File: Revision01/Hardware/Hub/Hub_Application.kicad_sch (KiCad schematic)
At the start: 81 parts, among them J10 IDC 6Pin Male Header, J11 IDC 6Pin Male Header, J12 IDC 6Pin Male Header, J13 IDC 6Pin Male Header, J14 IDC 6Pin Male Header, J15 IDC 6Pin Female Socket, J16 IDC 6Pin Male Header, J17 IDC 6Pin Female Socket, J18 IDC 6Pin Female Socket, J19 SMA-J-P-H-ST-EM1, J6 IDC 6Pin Male Header, J7 IDC 6Pin Male Header, J8 IDC 6Pin Male Header, J9 IDC 6Pin Male Header, Q1 PMOS, Q2 NMOS, Q3 PMOS, U3 MPU-6500, U4 Adafruit 3070

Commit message: . Merged Amplifier & Hub libraries into "Lib" . Added Amplifier 6 pin IDC footprint . Finalized Amplifier layout & silkscreen
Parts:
- J10, J11, J12, J13, J14, J16, J6, J7, J8, J9: footprint Hub:AdamTech_BHR-06-VUA -> Lib:AdamTech_BHR-06-VUA; symbol Hub:IDC_6Pin_Male_Header -> Lib:IDC_6Pin_Male_Header
- J15, J17, J18: symbol Hub:IDC_6Pin_Female_Socket -> Lib:IDC_6Pin_Female_Socket
- J19: symbol Hub:ANT_SMA_Edge -> Lib:ANT_SMA_Edge
- R10: symbol Hub:StrainGaugeFullBridge -> Lib:StrainGaugeFullBridge
- U3: footprint Hub:MPU-6500_QFN40P300X300X95-25N -> Lib:MPU-6500_QFN40P300X300X95-25N; symbol Hub:MPU-6500 -> Lib:MPU-6500
- U4: footprint Hub:Adafruit3070 -> Lib:Adafruit3070; symbol Hub:Adafruit3070 -> Lib:Adafruit3070
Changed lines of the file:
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@@
 	)
 	(symbol
-		(lib_id "Hub:IDC_6Pin_Male_Header")
+		(lib_id "Lib:IDC_6Pin_Male_Header")
 		(at 163.83 199.39 0)
 		(unit 1)
@@
 			)
 		)
-		(property "Footprint" "Hub:AdamTech_BHR-06-VUA"
+		(property "Footprint" "Lib:AdamTech_BHR-06-VUA"
 			(at 163.83 199.39 0)
 			(effects
@@
 	)
 	(symbol
-		(lib_id "Hub:IDC_6Pin_Male_Header")
+		(lib_id "Lib:IDC_6Pin_Male_Header")
 		(at 148.59 118.11 0)
 		(unit 1)
@@
 			)
 		)
-		(property "Footprint" "Hub:AdamTech_BHR-06-VUA"
+		(property "Footprint" "Lib:AdamTech_BHR-06-VUA"
 			(at 148.59 118.11 0)
 			(effects
@@
 	)
 	(symbol
-		(lib_id "Hub:IDC_6Pin_Male_Header")
+		(lib_id "Lib:IDC_6Pin_Male_Header")
 		(at 148.59 80.01 0)
 		(unit 1)
@@
 			)
 		)
-		(property "Footprint" "Hub:AdamTech_BHR-06-VUA"
+		(property "Footprint" "Lib:AdamTech_BHR-06-VUA"
 			(at 148.59 80.01 0)
 			(effects
@@
 	)
 	(symbol
-		(lib_id "Hub:IDC_6Pin_Male_Header")
+		(lib_id "Lib:IDC_6Pin_Male_Header")
 		(at 148.59 105.41 0)
 		(unit 1)
@@
 			)
 		)
-		(property "Footprint" "Hub:AdamTech_BHR-06-VUA"
+		(property "Footprint" "Lib:AdamTech_BHR-06-VUA"
 			(at 148.59 105.41 0)
 			(effects
@@
 	)
 	(symbol
-		(lib_id "Hub:ANT_SMA_Edge")
+		(lib_id "Lib:ANT_SMA_Edge")
 		(at 349.25 203.2 0)
 		(unit 1)
@@
 	)
 	(symbol
-		(lib_id "Hub:Adafruit3070")
+		(lib_id "Lib:Adafruit3070")
 		(at 285.75 179.07 0)
 		(unit 1)
@@
 			)
 		)
-		(property "Footprint" "Hub:Adafruit3070"
+		(property "Footprint" "Lib:Adafruit3070"
 			(at 285.75 179.07 0)
 			(effects
@@
 	)
 	(symbol
-		(lib_id "Hub:IDC_6Pin_Male_Header")
+		(lib_id "Lib:IDC_6Pin_Male_Header")
 		(at 148.59 168.91 0)
 		(unit 1)
@@
 			)
 		)
-		(property "Footprint" "Hub:AdamTech_BHR-06-VUA"
+		(property "Footprint" "Lib:AdamTech_BHR-06-VUA"
 			(at 148.59 168.91 0)
 			(effects
@@
 	)
 	(symbol
-		(lib_id "Hub:StrainGaugeFullBridge")
+		(lib_id "Lib:StrainGaugeFullBridge")
 		(at 146.05 57.15 0)
 		(unit 1)
@@
 	)
 	(symbol
-		(lib_id "Hub:IDC_6Pin_Male_Header")
+		(lib_id "Lib:IDC_6Pin_Male_Header")
 		(at 199.39 199.39 0)
 		(unit 1)
@@
 			)
 		)
-		(property "Footprint" "Hub:AdamTech_BHR-06-VUA"
+		(property "Footprint" "Lib:AdamTech_BHR-06-VUA"
 			(at 199.39 199.39 0)
 			(effects
@@
 	)
 	(symbol
-		(lib_id "Hub:IDC_6Pin_Female_Socket")
+		(lib_id "Lib:IDC_6Pin_Female_Socket")
 		(at 181.61 199.39 0)
 		(mirror y)
@@
 	)
 	(symbol
-		(lib_id "Hub:IDC_6Pin_Male_Header")
+		(lib_id "Lib:IDC_6Pin_Male_Header")
 		(at 148.59 143.51 0)
 		(unit 1)
@@
 			)
 		)
-		(property "Footprint" "Hub:AdamTech_BHR-06-VUA"
+		(property "Footprint" "Lib:AdamTech_BHR-06-VUA"
 			(at 148.59 143.51 0)
 			(effects
@@
 	)
 	(symbol
-		(lib_id "Hub:MPU-6500")
+		(lib_id "Lib:MPU-6500")
 		(at 321.31 110.49 0)
 		(unit 1)
@@
 			)
 		)
-		(property "Footprint" "Hub:MPU-6500_QFN40P300X300X95-25N"
+		(property "Footprint" "Lib:MPU-6500_QFN40P300X300X95-25N"
 			(at 321.31 93.98 0)
 			(effects
@@
 	)
 	(symbol
-		(lib_id "Hub:IDC_6Pin_Female_Socket")
+		(lib_id "Lib:IDC_6Pin_Female_Socket")
 		(at 218.44 199.39 0)
 		(mirror y)
@@
 	)
 	(symbol
-		(lib_id "Hub:IDC_6Pin_Male_Header")
+		(lib_id "Lib:IDC_6Pin_Male_Header")
 		(at 148.59 92.71 0)
 		(unit 1)
@@
 			)
 		)
-		(property "Footprint" "Hub:AdamTech_BHR-06-VUA"
+		(property "Footprint" "Lib:AdamTech_BHR-06-VUA"
 			(at 148.59 92.71 0)
 			(effects
@@
 	)
 	(symbol
-		(lib_id "Hub:IDC_6Pin_Male_Header")
+		(lib_id "Lib:IDC_6Pin_Male_Header")
 		(at 148.59 156.21 0)
 		(unit 1)
@@
 			)
 		)
-		(property "Footprint" "Hub:AdamTech_BHR-06-VUA"
+		(property "Footprint" "Lib:AdamTech_BHR-06-VUA"
 			(at 148.59 156.21 0)
 			(effects
@@
 	)
 	(symbol
-		(lib_id "Hub:IDC_6Pin_Female_Socket")
+		(lib_id "Lib:IDC_6Pin_Female_Socket")
 		(at 231.14 199.39 0)
 		(unit 1)
@@
 	)
 	(symbol
-		(lib_id "Hub:IDC_6Pin_Male_Header")
+		(lib_id "Lib:IDC_6Pin_Male_Header")
 		(at 148.59 130.81 0)
 		(unit 1)
@@
 			)
 		)
-		(property "Footprint" "Hub:AdamTech_BHR-06-VUA"
+		(property "Footprint" "Lib:AdamTech_BHR-06-VUA"
 			(at 148.59 130.81 0)
 			(effects

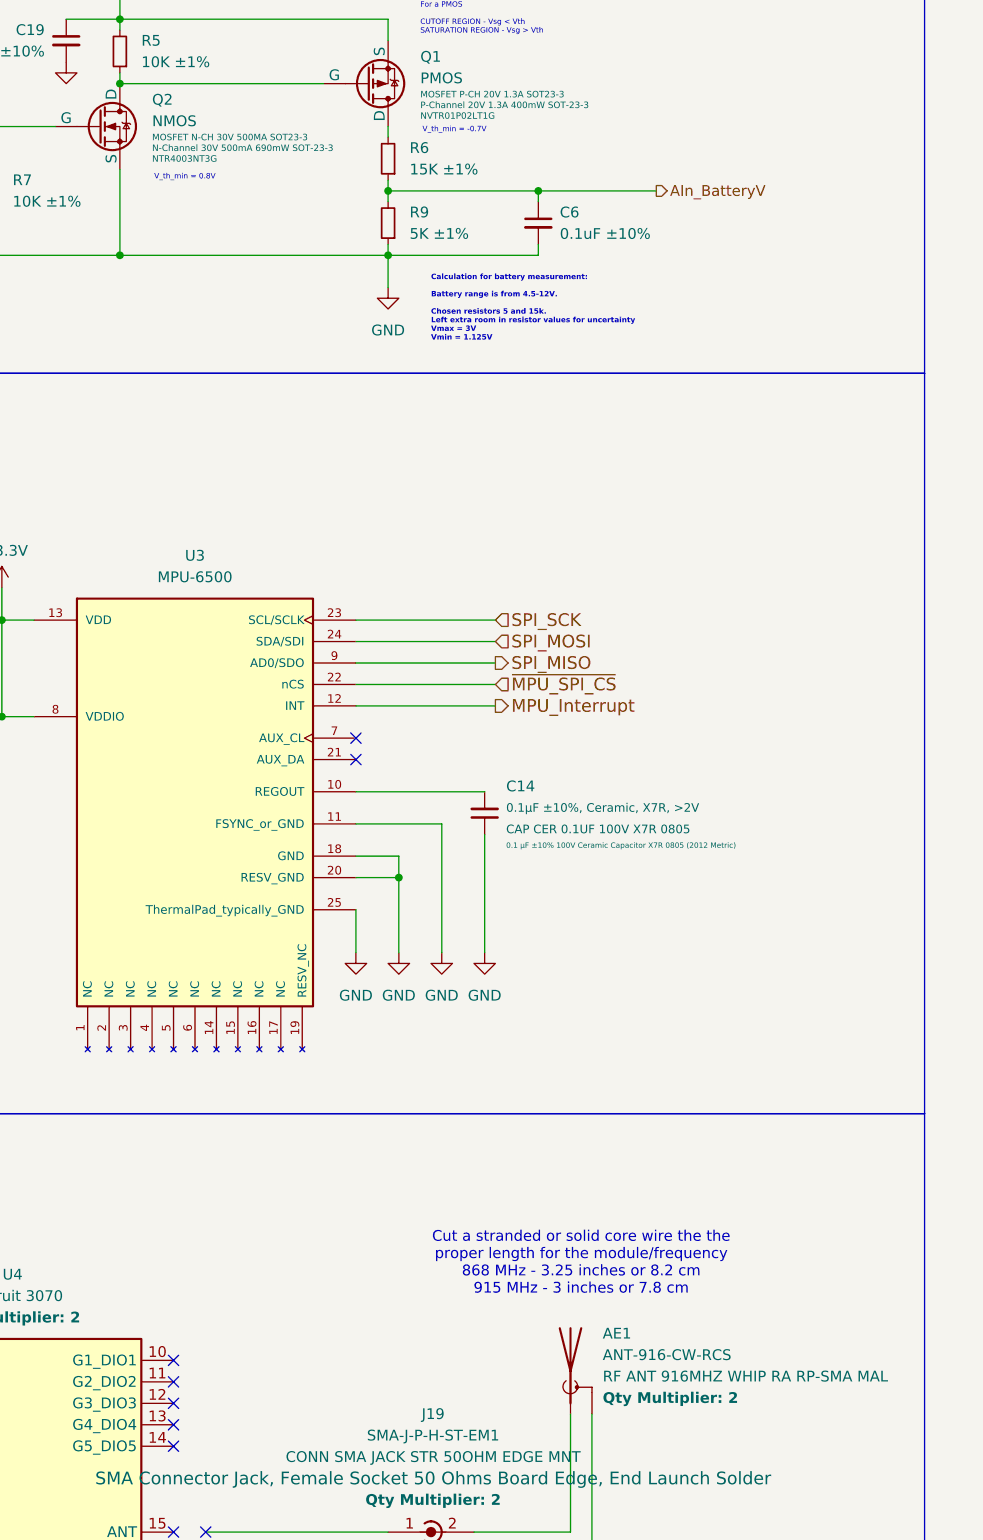
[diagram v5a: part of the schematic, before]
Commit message: . Fixed major BOM bug in Antenna, ordering correct Male Outer, Male Inner Part . Added Mouser column in Hub.
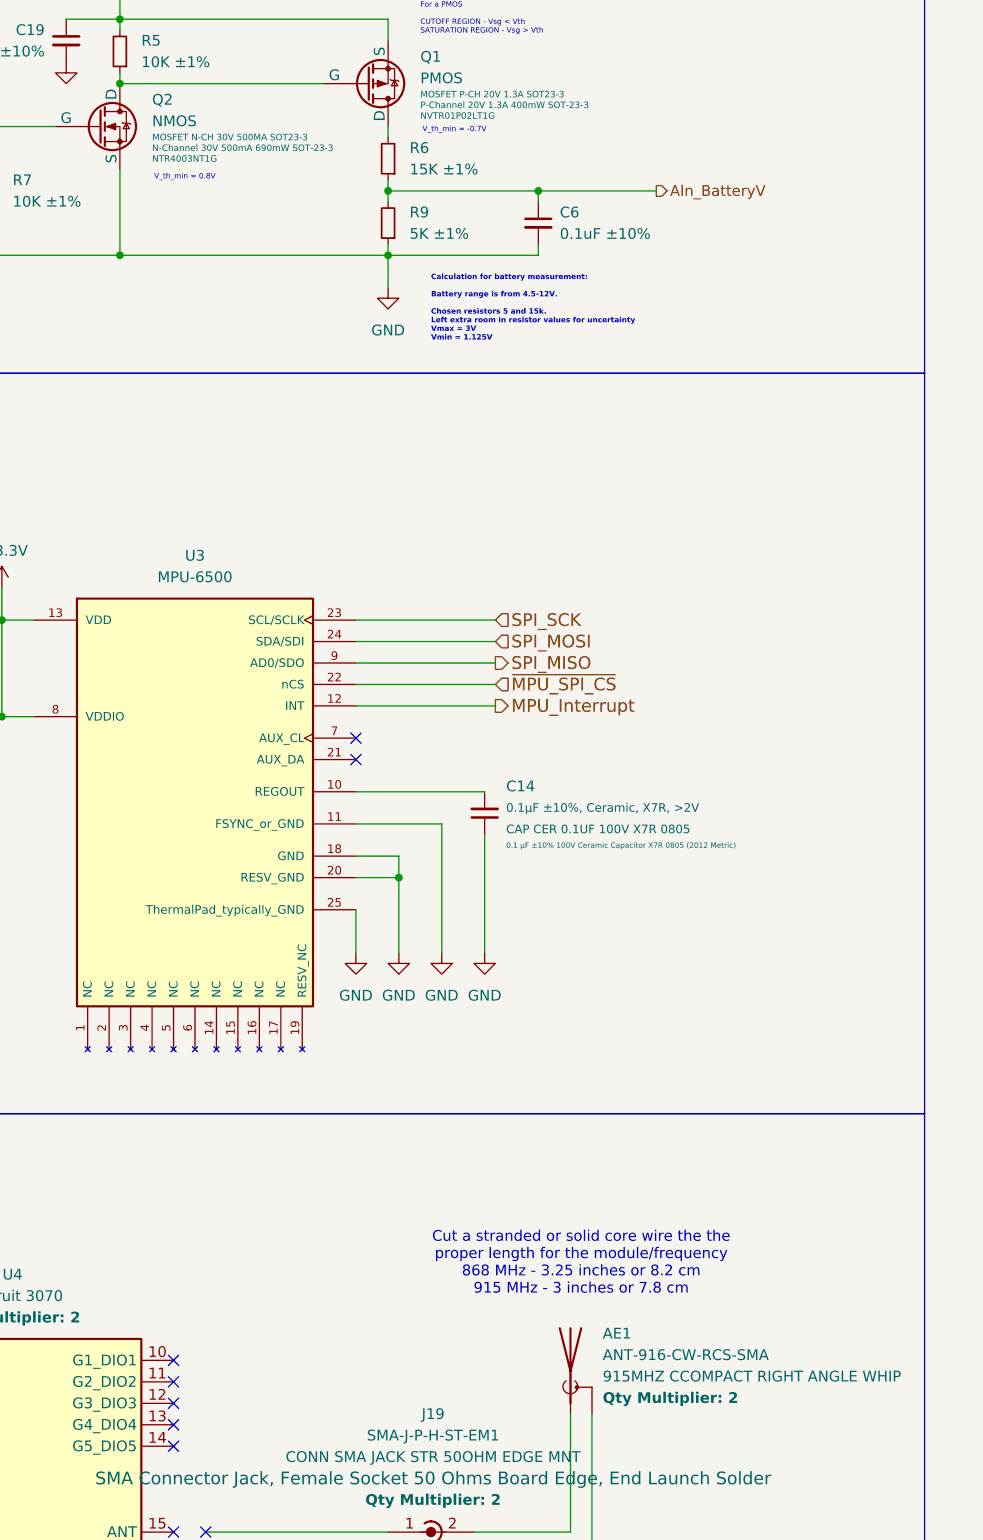
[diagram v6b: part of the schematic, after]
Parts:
- AE1: value ANT-916-CW-RCS -> ANT-916-CW-RCS-SMA; Detailed Description RF ANTENNA ISM, LoRa, Sensor Networks, SigFox Whip, Right A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 -> RF ANTENNA ISM, LoRaWAN, LPWA Whip, Right Angle SMA Male Co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; DigiKey Link https://www.digikey.ca/en/products/detail/te-connectivity-linx/ANT-916-CW-RCS/340139 -> https://www.digikey.ca/en/products/detail/te-connectivity-linx/ANT-916-CW-RCS-SMA/16630288?s=N4IgTCBcDaIIIDkAqBaAnARgGwoMIHUUAlXAZRVIFk4QBdAXyA; DigiKey Part Number ANT-916-CW-RCS-ND -> 343-ANT-916-CW-RCS-SMA-ND; Manufacturer Part Number ANT-916-CW-RCS -> ANT-916-CW-RCS-SMA; Mouser Link (none) -> https://www.mouser.ca/ProductDetail/TE-Connectivity-Linx-Te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; Mouser Part Number (none) -> 712-ANT-916-CWRCSSMA
- C1, C19: Mouser Link (none) -> https://www.mouser.ca/ProductDetail/Samsung-Electro-Mechani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; Mouser Part Number (none) -> 187-CL31A226KAHNNNE
- C10, C14, C6, C7: Mouser Link (none) -> https://www.mouser.ca/ProductDetail/Samsung-Electro-Mechani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; Mouser Part Number (none) -> 187-CL21B104KCFNNNE
- C12: Mouser Link (none) -> https://www.mouser.ca/ProductDetail/Samsung-Electro-Mechani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; Mouser Part Number (none) -> 187-CL10B103KB8WPND
- D1, D10, D11, D12, D13, D14, D15, D16, D2, D3, D4, D5, D6, D7, D8, D9: Mouser Link (none) -> https://www.mouser.ca/ProductDetail/Diodes-Incorporated/DDZ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; Mouser Part Number (none) -> 621-DDZ9684-7
- F2, F3, F4, F5, F6, F7, F8, F9: Mouser Link (none) -> https://www.mouser.ca/ProductDetail/KYOCERA-AVX/F0603G0R02F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; Mouser Part Number (none) -> 581-F0603G0R02FNTR
- J10, J11, J12, J13, J14, J16, J6, J7, J8, J9: Mouser Link (none) -> https://www.mouser.ca/ProductDetail/Adam-Tech/BHR-06-VUA?qs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; Mouser Part Number (none) -> 737-BHR-06-VUA
- J15, J17, J18: Mouser Link (none) -> https://www.mouser.ca/ProductDetail/Adam-Tech/FCS-06-SG?qs=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; Mouser Part Number (none) -> 737-FCS-06-SG
- J19: Mouser Link (none) -> https://www.mouser.ca/ProductDetail/Samtec/SMA-J-P-H-ST-EM1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; Mouser Part Number (none) -> SMA-J-P-H-ST-EM1
- Q1: Mouser Link (none) -> https://www.mouser.ca/ProductDetail/onsemi/NVTR01P02LT1G?qs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; Mouser Part Number (none) -> 863-NVTR01P02LT1G
- Q2: Manufacturer Part Number NTR4003NT3G -> NTR4003NT1G; Mouser Link (none) -> https://www.mouser.ca/ProductDetail/onsemi/NTR4003NT1G?qs=C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; Mouser Part Number (none) -> 863-NTR4003NT1G
- Q3: Mouser Link (none) -> https://www.mouser.ca/ProductDetail/Diodes-Incorporated/ZXM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; Mouser Part Number (none) -> 522-ZXMP10A13FTA
- R11, R13, R15, R17, R19, R2, R21, R23: Mouser Link (none) -> https://www.mouser.ca/ProductDetail/Vishay/CRCW0805100RFKEA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; Mouser Part Number (none) -> 71-CRCW0805-100-E3
- R12, R14, R16, R18, R20, R22, R24, R26: Mouser Link (none) -> https://www.mouser.ca/ProductDetail/Vishay/CRCW08051M00FKEA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; Mouser Part Number (none) -> 71-CRCW0805-1.0M-E3
- R5, R7, R8: Mouser Link (none) -> https://www.mouser.ca/ProductDetail/Vishay/CRCW080510K0FKEA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; Mouser Part Number (none) -> 71-CRCW0805-10K-E3
- R6: Mouser Link (none) -> https://www.mouser.ca/ProductDetail/Vishay/CRCW080515K0FKEA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; Mouser Part Number (none) -> 71-CRCW0805-15K-E3
- R9: Mouser Link (none) -> https://www.mouser.ca/ProductDetail/Vishay/CRCW08055K00FKTA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; Mouser Part Number (none) -> 71-CRCW0805-5K
- U3: Mouser Link (none) -> https://www.mouser.ca/ProductDetail/TDK-InvenSense/MPU-6500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; Mouser Part Number (none) -> 410-MPU-6500
- U4: Mouser Link (none) -> https://www.mouser.ca/ProductDetail/Adafruit/3070?qs=AGnqjq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; Mouser Part Number (none) -> 485-3070

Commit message: . Exported BOM (.csv), gerbers & dill files, 3D Model (.step) file to Product/2025-08-16 for both Amplifier & Hub boards.
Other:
- company: BCIT BAJA -> BCIT Racing
- title: Peripherals -> Hub
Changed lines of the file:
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@@
 	(paper "A3")
 	(title_block
-		(title "Peripherals")
-		(date "2025-03-08")
-		(rev "1")
-		(company "BCIT BAJA")
+		(title "Hub")
+		(date "2025-08-16")
+		(rev "01")
+		(company "BCIT Racing")
+		(comment 1 "Parry Zhuo & Daniel Mahmoud")
 	)
 	(rectangle

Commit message: . Made sure amplifier passive silk screen doesn't overlap pads . Added 6xAA battery holder to hub BOM . Exported gerbers, drl files .zip (PCBWay approved)
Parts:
- C1, C19: DigiKey Part Number 1276-3047-1-ND - Cut Tape (CT) -> 1276-3047-1-ND
- C10, C14: value 0.1µF ±10%, Ceramic, X7R, >2V -> 0.1uF ±10%, X7R; DigiKey Part Number 1276-6840-1-ND - Cut Tape (CT) -> 1276-6840-1-ND
- C11, C13, C15, C16, C17, C18, C8, C9: DigiKey Link (none) -> https://www.digikey.ca/en/products/detail/samsung-electro-m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; DigiKey Part Number (none) -> 1276-1185-2-ND
- C12: DigiKey Part Number 1276-CL10B103KB8WPNDCT-ND - Cut Tape (CT) -> 1276-CL10B103KB8WPNDCT-ND
- C6, C7: value 0.1uF ±10% -> 0.1uF ±10%, X7R; DigiKey Part Number 1276-6840-1-ND - Cut Tape (CT) -> 1276-6840-1-ND
- F2, F3, F4, F5, F6, F7, F8, F9: DigiKey Part Number 478-13097-1-ND - Cut Tape (CT) -> 478-13097-1-ND
- J19: value SMA-J-P-H-ST-EM1 -> CON-SMA-EDGE-S; Detailed Description SMA Connector Jack, Female Socket 50 Ohms Board Edge, End L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 -> SMA Connector Jack, Female Socket Board Edge, End Launch So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; DigiKey Link https://www.digikey.ca/en/products/detail/samtec-inc/SMA-J-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 -> https://www.digikey.ca/en/products/detail/rf-solutions/CON-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; DigiKey Part Number SAM8857-ND -> CON-SMA-EDGE-S-ND; Manufacturer Samtec Inc. -> RF Solutions; Manufacturer Part Number SMA-J-P-H-ST-EM1 -> CON-SMA-EDGE-S; Mouser Link https://www.mouser.ca/ProductDetail/Samtec/SMA-J-P-H-ST-EM1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 -> https://www.mouser.ca/ProductDetail/RF-Solutions/CON-SMA-ED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; Mouser Part Number SMA-J-P-H-ST-EM1 -> 223-CON-SMA-EDGE-S
- Q2: DigiKey Part Number NTR4003NT3GOSCT-ND - Cut Tape (CT) -> NTR4003NT3GOSCT-ND
- R10: DigiKey Link https://www.aliexpress.com/item/1005006546478858.html -> (none)
- R11, R13, R15, R17, R19, R2, R21, R23: DigiKey Part Number 541-100CCT-ND - Cut Tape (CT) -> 541-100CCT-ND
- R12, R14, R16, R18, R20, R22, R24, R26: DigiKey Part Number 541-1.00MCCT-ND - Cut Tape (CT) -> 541-1.00MCCT-ND
- R5, R7, R8: DigiKey Part Number 541-10.0KCCT-ND - Cut Tape (CT) -> 541-10.0KCCT-ND
- R6: DigiKey Part Number 541-15.0KCCT-ND - Cut Tape (CT) -> 541-15.0KCCT-ND
- R9: DigiKey Part Number 541-CRCW08055K00FKTACT-ND - Cut Tape (CT) -> 541-CRCW08055K00FKTACT-ND
- U3: DigiKey Part Number 1428-1011-1-ND - Cut Tape (CT) -> 1428-1011-1-ND
